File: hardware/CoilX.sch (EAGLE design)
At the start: 13 parts, among them U1 74AHC1G14DBV, U2 TLP283

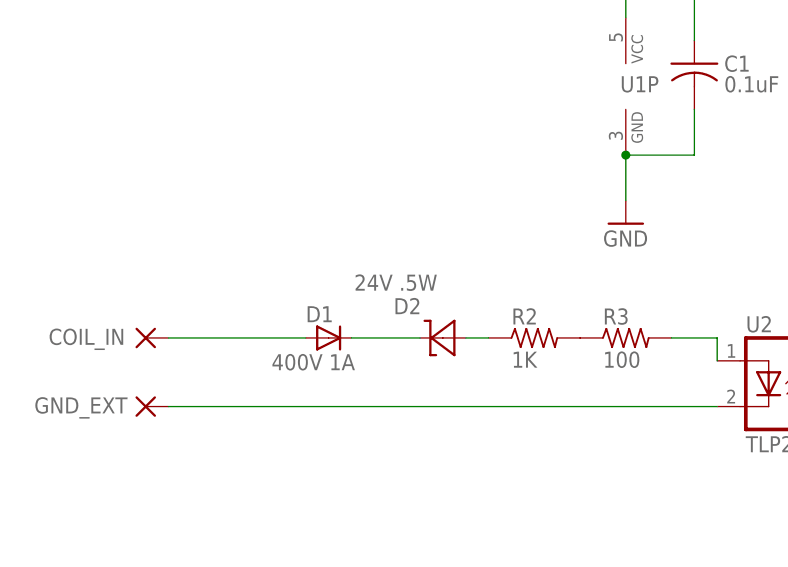
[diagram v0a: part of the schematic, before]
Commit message: changed zener diode to 75v
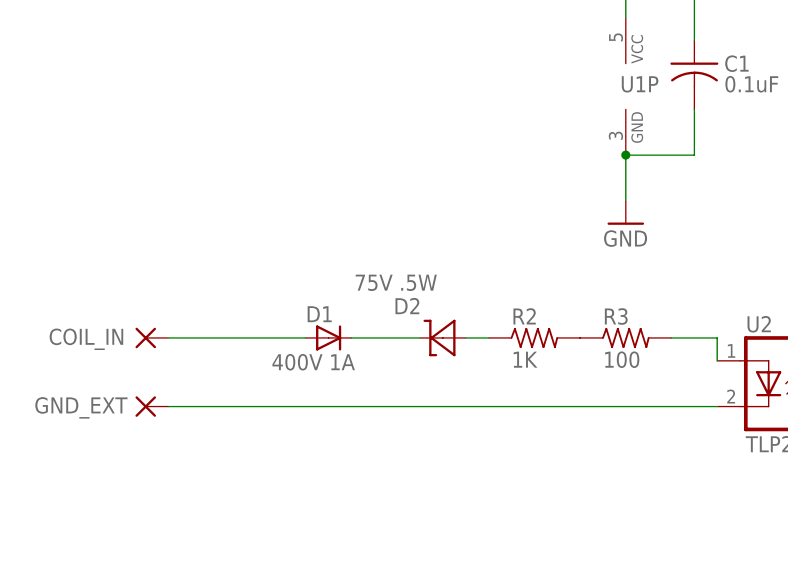
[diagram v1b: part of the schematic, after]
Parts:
- D2: value 24V .5W -> 75V .5W
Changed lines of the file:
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@@
 <part name="U2" library="optocoupler" deviceset="TLP283" device=""/>
 <part name="R2" library="rcl" deviceset="R-US_" device="R1206" value="1K"/>
-<part name="D2" library="smt_diodes" deviceset="ZENER" device="2" value="24V .5W"/>
+<part name="D2" library="smt_diodes" deviceset="ZENER" device="2" value="75V .5W"/>
 <part name="R1" library="rcl" deviceset="R-US_" device="R0603" value="10K"/>
 <part name="P+27" library="supply1" deviceset="+5V" device=""/>

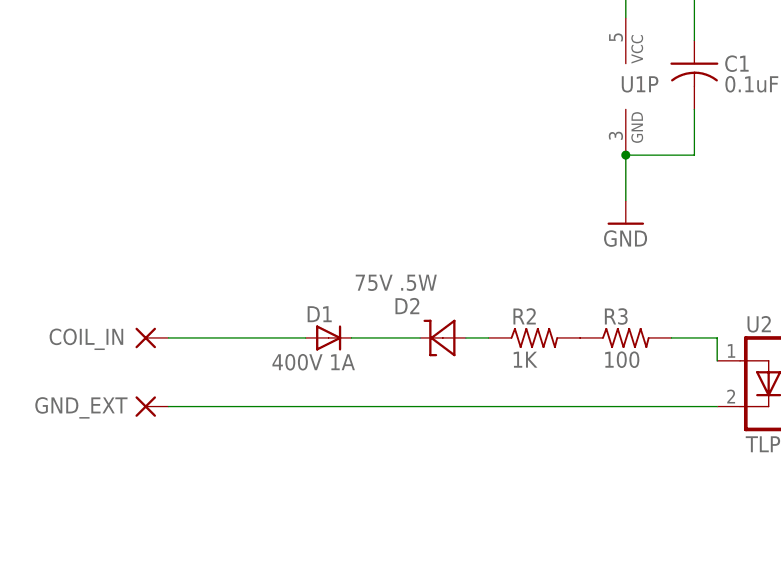
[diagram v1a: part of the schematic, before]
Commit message: updated zener to 110v
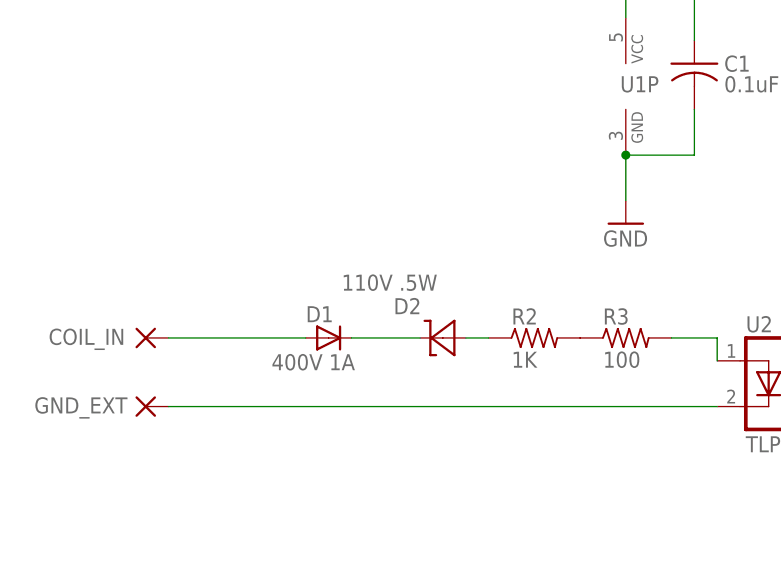
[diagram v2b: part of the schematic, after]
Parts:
- D2: value 75V .5W -> 110V .5W
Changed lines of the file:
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@@
 <?xml version="1.0" encoding="utf-8"?>
 <!DOCTYPE eagle SYSTEM "eagle.dtd">
-<eagle version="6.5.0">
+<eagle version="7.2.0">
 <drawing>
 <settings>
@@
 <part name="U2" library="optocoupler" deviceset="TLP283" device=""/>
 <part name="R2" library="rcl" deviceset="R-US_" device="R1206" value="1K"/>
-<part name="D2" library="smt_diodes" deviceset="ZENER" device="2" value="75V .5W"/>
+<part name="D2" library="smt_diodes" deviceset="ZENER" device="2" value="110V .5W"/>
 <part name="R1" library="rcl" deviceset="R-US_" device="R0603" value="10K"/>
 <part name="P+27" library="supply1" deviceset="+5V" device=""/>
